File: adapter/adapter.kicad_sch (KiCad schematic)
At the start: 18 parts, among them J1 Conn_01x03_Female, J2 Conn_01x06_Female, SW1 RotaryEncoder_Switch

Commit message: routing, add R C
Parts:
- removed R2: R, Resistor_SMD:R_1206_3216Metric_Pad1.42x1.75mm_HandSolder, symbol Device:R
- C1: footprint Capacitor_SMD:C_1206_3216Metric_Pad1.42x1.75mm_HandSolder -> Capacitor_SMD:C_1206_3216Metric_Pad1.33x1.80mm_HandSolder
- R1: footprint Resistor_SMD:R_1206_3216Metric_Pad1.42x1.75mm_HandSolder -> Resistor_SMD:R_1206_3216Metric_Pad1.30x1.75mm_HandSolder
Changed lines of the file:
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@@
   (junction (at 118.11 102.87) (diameter 1.016) (color 0 0 0 0)
   )
-  (junction (at 73.914 95.25) (diameter 1.016) (color 0 0 0 0)
-  )
   (junction (at 30.226 34.29) (diameter 0) (color 0 0 0 0)
   )
@@
   )
   (junction (at 212.09 102.87) (diameter 0) (color 0 0 0 0)
-  )
-  (junction (at 81.534 95.25) (diameter 0) (color 0 0 0 0)
   )
   (junction (at 137.16 87.63) (diameter 0) (color 0 0 0 0)
@@
     (stroke (width 0) (type default) (color 0 0 0 0))
   )
-  (wire (pts (xy 81.534 97.79) (xy 81.534 95.25))
-    (stroke (width 0) (type solid) (color 0 0 0 0))
-  )
   (wire (pts (xy 88.9 87.63) (xy 97.79 87.63))
     (stroke (width 0) (type default) (color 0 0 0 0))
@@
   (wire (pts (xy 112.268 124.714) (xy 129.286 124.714))
     (stroke (width 0) (type default) (color 0 0 0 0))
-  )
-  (wire (pts (xy 73.914 95.25) (xy 73.914 97.79))
-    (stroke (width 0) (type solid) (color 0 0 0 0))
   )
   (wire (pts (xy 112.268 109.474) (xy 129.286 109.474))
@@
     (property "Reference" "R1" (id 0) (at 77.724 90.17 90))
     (property "Value" "R" (id 1) (at 77.724 92.71 90))
-    (property "Footprint" "Resistor_SMD:R_1206_3216Metric_Pad1.42x1.75mm_HandSolder" (id 2) (at 77.724 93.472 90)
+    (property "Footprint" "Resistor_SMD:R_1206_3216Metric_Pad1.30x1.75mm_HandSolder" (id 2) (at 77.724 93.472 90)
       (effects (font (size 1.27 1.27)) hide)
     )
@@
     (pin "1")
   )
-  (symbol (lib_id "Device:R") (at 77.724 97.79 270) (unit 1)
-    (in_bom yes) (on_board yes)
-    (property "Reference" "R2" (id 0) (at 77.724 92.71 90))
-    (property "Value" "R" (id 1) (at 77.724 95.25 90))
-    (property "Footprint" "Resistor_SMD:R_1206_3216Metric_Pad1.42x1.75mm_HandSolder" (id 2) (at 77.724 96.012 90)
-      (effects (font (size 1.27 1.27)) hide)
-    )
-    (property "Datasheet" "~" (id 3) (at 77.724 97.79 0)
-      (effects (font (size 1.27 1.27)) hide)
-    )
-    (pin "1")
-    (pin "2")
-  )
   (symbol (lib_id "power:+5V") (at 30.226 26.67 90) (unit 1)
     (in_bom yes) (on_board yes)
@@
       (effects (font (size 1.27 1.27)) (justify left))
     )
-    (property "Footprint" "Capacitor_SMD:C_1206_3216Metric_Pad1.42x1.75mm_HandSolder" (id 2) (at 37.5412 96.266 0)
+    (property "Footprint" "Capacitor_SMD:C_1206_3216Metric_Pad1.33x1.80mm_HandSolder" (id 2) (at 37.5412 96.266 0)
       (effects (font (size 1.27 1.27)) hide)
     )
@@
     )
     (path "/b720e53b-ae72-4295-b3ff-de5411507232"
-      (reference "C1") (unit 1) (value "1u") (footprint "Capacitor_SMD:C_1206_3216Metric_Pad1.42x1.75mm_HandSolder")
+      (reference "C1") (unit 1) (value "1u") (footprint "Capacitor_SMD:C_1206_3216Metric_Pad1.33x1.80mm_HandSolder")
     )
     (path "/223b04e8-40ea-4e7c-a2bb-67f20935b256"
@@
     )
     (path "/3145c452-dc50-487a-9802-6b13d8b48c50"
-      (reference "R1") (unit 1) (value "R") (footprint "Resistor_SMD:R_1206_3216Metric_Pad1.42x1.75mm_HandSolder")
-    )
-    (path "/890ed13f-42f7-4528-85cf-e8c0911e8d2e"
-      (reference "R2") (unit 1) (value "R") (footprint "Resistor_SMD:R_1206_3216Metric_Pad1.42x1.75mm_HandSolder")
+      (reference "R1") (unit 1) (value "R") (footprint "Resistor_SMD:R_1206_3216Metric_Pad1.30x1.75mm_HandSolder")
     )
     (path "/d31898a0-dde3-4548-9b2f-a263c96d031c"

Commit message: license
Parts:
- removed J1: Conn_01x03_Female, Connector_PinHeader_2.54mm:PinHeader_1x03_P2.54mm_Vertical, symbol Connector:Conn_01x03_Female
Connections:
- net GND: no longer C1.2, D1.2 (VSS), D10.2 (VSS), D11.2 (VSS), D12.2 (VSS), D2.2 (VSS), D3.2 (VSS), D4.2 (VSS), D5.2 (VSS), D6.2 (VSS), D7.2 (VSS), D8.2 (VSS), D9.2 (VSS)
- new net Gnd: C1.2, D1.2 (VSS), D10.2 (VSS), D11.2 (VSS), D12.2 (VSS), D2.2 (VSS), D3.2 (VSS), D4.2 (VSS), D5.2 (VSS), D6.2 (VSS), D7.2 (VSS), D8.2 (VSS), D9.2 (VSS)
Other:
- note added: "This work is licensed under a Creative Commons Attribution-NonCommercial-ShareAlike 4.0 International License."
- note removed: "RGB"
- company: BastardKB x KarlK90 -> BastardKB
- title: Charybdis Blackpill Holder -> Charybdis Rotary Encoder
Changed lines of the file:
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@@
   (paper "A4")
   (title_block
-    (title "Charybdis Blackpill Holder")
-    (date "2022-01-20")
-    (rev "1.2")
-    (company "BastardKB x KarlK90")
+    (title "Charybdis Rotary Encoder")
+    (date "2022-01-26")
+    (rev "1.0")
+    (company "BastardKB")
     (comment 1 "Licensed under CERN-OHL-W v2")
   )
@@
   )
   (junction (at 112.268 124.714) (diameter 0) (color 0 0 0 0)
-  )
-  (junction (at 26.162 73.66) (diameter 0) (color 0 0 0 0)
   )
   (junction (at 80.264 102.87) (diameter 0) (color 0 0 0 0)
@@
     (stroke (width 0) (type default) (color 0 0 0 0))
   )
-  (wire (pts (xy 26.162 73.66) (xy 34.29 73.66))
-    (stroke (width 0) (type default) (color 0 0 0 0))
-  )
-  (wire (pts (xy 26.162 73.66) (xy 26.162 75.184))
-    (stroke (width 0) (type default) (color 0 0 0 0))
-  )
   (wire (pts (xy 112.268 124.714) (xy 129.286 124.714))
     (stroke (width 0) (type default) (color 0 0 0 0))
@@
     (stroke (width 0) (type default) (color 0 0 0 0))
   )
-  (wire (pts (xy 24.13 73.66) (xy 26.162 73.66))
-    (stroke (width 0) (type default) (color 0 0 0 0))
-  )
   (wire (pts (xy 137.16 102.87) (xy 154.94 102.87))
     (stroke (width 0) (type default) (color 0 0 0 0))
@@
     (effects (font (size 1.27 1.27)) (justify left bottom))
   )
-  (text "RGB" (at 21.59 67.31 0)
-    (effects (font (size 1.27 1.27)) (justify left bottom))
+  (text "This work is licensed under a Creative Commons Attribution-NonCommercial-ShareAlike 4.0 International License."
+    (at 279.4 163.83 0)
+    (effects (font (size 1.27 1.27)) (justify right bottom))
   )
   (global_label "Vcc" (shape input) (at 26.924 34.29 180)
@@
     )
   )
-  (global_label "Din" (shape input) (at 34.29 76.2 180)
-    (effects (font (size 1.27 1.27)) (justify right))
-    (property "Intersheet References" "${INTERSHEET_REFS}" (id 0) (at -2.54 2.54 0)
-      (effects (font (size 1.27 1.27)) hide)
-    )
-  )
   (global_label "r1" (shape input) (at 92.71 35.56 0) (fields_autoplaced)
     (effects (font (size 1.1938 1.1938)) (justify left))
@@
     )
   )
-  (global_label "Vcc" (shape input) (at 34.29 71.12 180)
-    (effects (font (size 1.27 1.27)) (justify right))
-    (property "Intersheet References" "${INTERSHEET_REFS}" (id 0) (at -2.54 2.54 0)
-      (effects (font (size 1.27 1.27)) hide)
-    )
-  )
   (global_label "Vcc" (shape input) (at 30.734 87.884 180)
     (effects (font (size 1.27 1.27)) (justify right))
     (property "Intersheet References" "${INTERSHEET_REFS}" (id 0) (at -6.096 19.304 0)
-      (effects (font (size 1.27 1.27)) hide)
-    )
-  )
-  (global_label "Gnd" (shape input) (at 24.13 73.66 180)
-    (effects (font (size 1.27 1.27)) (justify right))
-    (property "Intersheet References" "${INTERSHEET_REFS}" (id 0) (at -12.7 2.54 0)
       (effects (font (size 1.27 1.27)) hide)
     )
@@
     (pin "1")
   )
-  (symbol (lib_id "power:GND") (at 26.162 75.184 0) (unit 1)
-    (in_bom yes) (on_board yes)
-    (property "Reference" "#PWR0104" (id 0) (at 26.162 81.534 0)
-      (effects (font (size 1.27 1.27)) hide)
-    )
-    (property "Value" "GND" (id 1) (at 26.162 78.994 0))
-    (property "Footprint" "" (id 2) (at 26.162 75.184 0)
-      (effects (font (size 1.27 1.27)) hide)
-    )
-    (property "Datasheet" "" (id 3) (at 26.162 75.184 0)
-      (effects (font (size 1.27 1.27)) hide)
-    )
-    (pin "1")
-  )
   (symbol (lib_id "Device:C") (at 36.576 92.456 0) (unit 1)
     (in_bom yes) (on_board yes)
@@
     (pin "S2")
   )
-  (symbol (lib_id "Connector:Conn_01x03_Female") (at 39.37 73.66 0) (unit 1)
-    (in_bom yes) (on_board yes)
-    (property "Reference" "J1" (id 0) (at 40.0813 72.9678 0)
-      (effects (font (size 1.27 1.27)) (justify left))
-    )
-    (property "Value" "Conn_01x03_Female" (id 1) (at 40.0813 75.2665 0)
-      (effects (font (size 1.27 1.27)) (justify left))
-    )
-    (property "Footprint" "Connector_PinHeader_2.54mm:PinHeader_1x03_P2.54mm_Vertical" (id 2) (at 39.37 73.66 0)
-      (effects (font (size 1.27 1.27)) hide)
-    )
-    (property "Datasheet" "~" (id 3) (at 39.37 73.66 0)
-      (effects (font (size 1.27 1.27)) hide)
-    )
-    (pin "1")
-    (pin "2")
-    (pin "3")
-  )
   (symbol (lib_id "power:GND") (at 75.946 41.402 0) (unit 1)
     (in_bom yes) (on_board yes)
@@
       (reference "#PWR0103") (unit 1) (value "GND") (footprint "")
     )
-    (path "/9fc3e7de-917d-471e-9baf-20e418f20549"
-      (reference "#PWR0104") (unit 1) (value "GND") (footprint "")
-    )
     (path "/f298f139-b4e7-4161-948f-e52265423988"
       (reference "#PWR0105") (unit 1) (value "GND") (footprint "")
@@
       (reference "D12") (unit 1) (value "SK6812MINI") (footprint "Library:YS-SK6812MINI-E")
     )
-    (path "/eb54f150-1815-419c-99e6-8c3c5774df70"
-      (reference "J1") (unit 1) (value "Conn_01x03_Female") (footprint "Connector_PinHeader_2.54mm:PinHeader_1x03_P2.54mm_Vertical")
-    )
     (path "/26af3975-a636-45c1-8b88-2ae79f76cdc4"

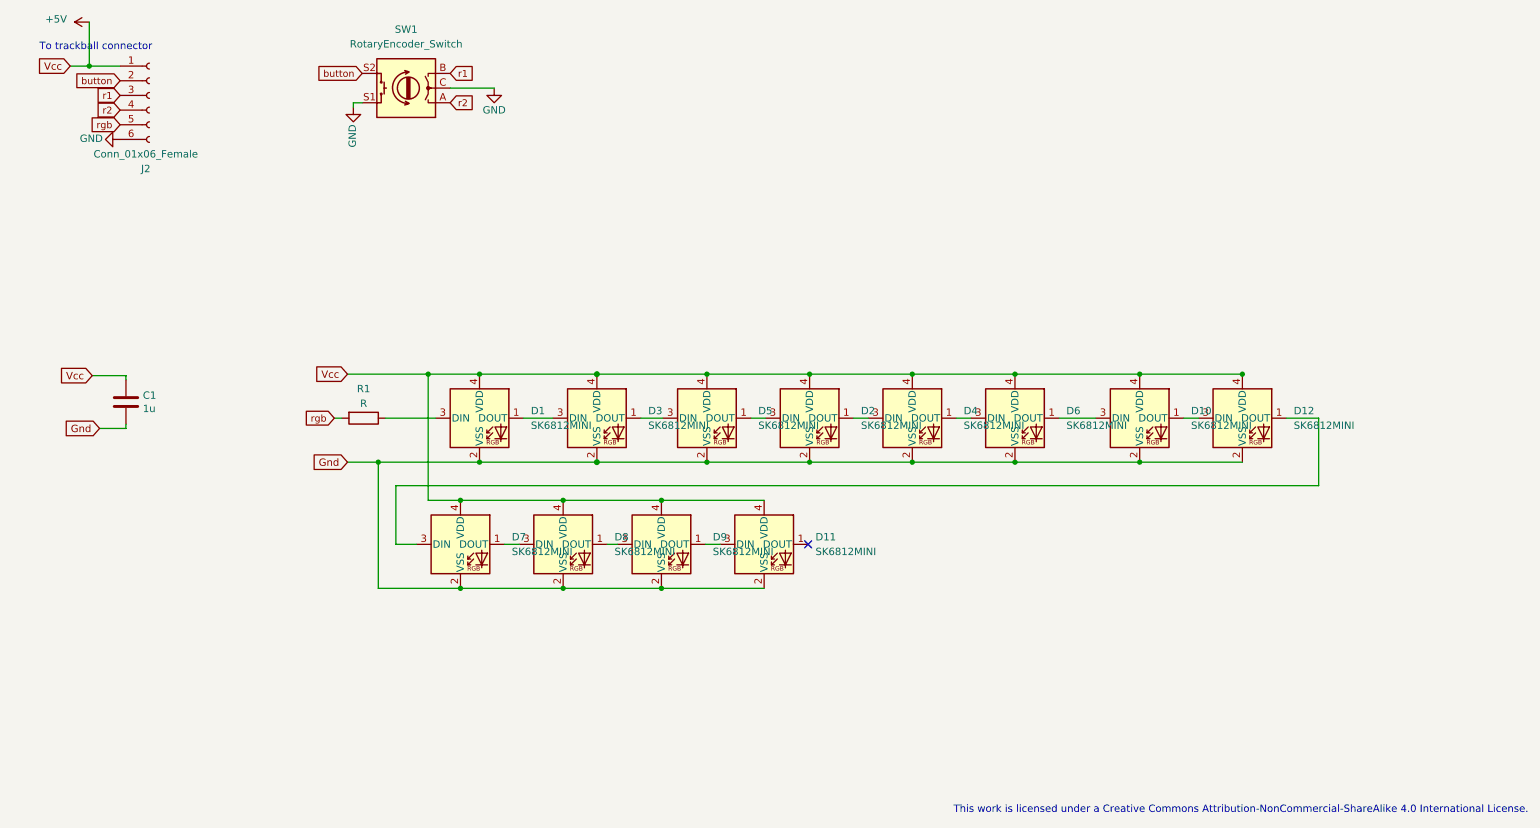
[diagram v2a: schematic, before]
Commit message: complete reroute
- routing changed to fix din/dout paths
- added dout header
- renamed rgb header to din
- moved SMT components to bottom side
- changed silkscreen to rev 1.1
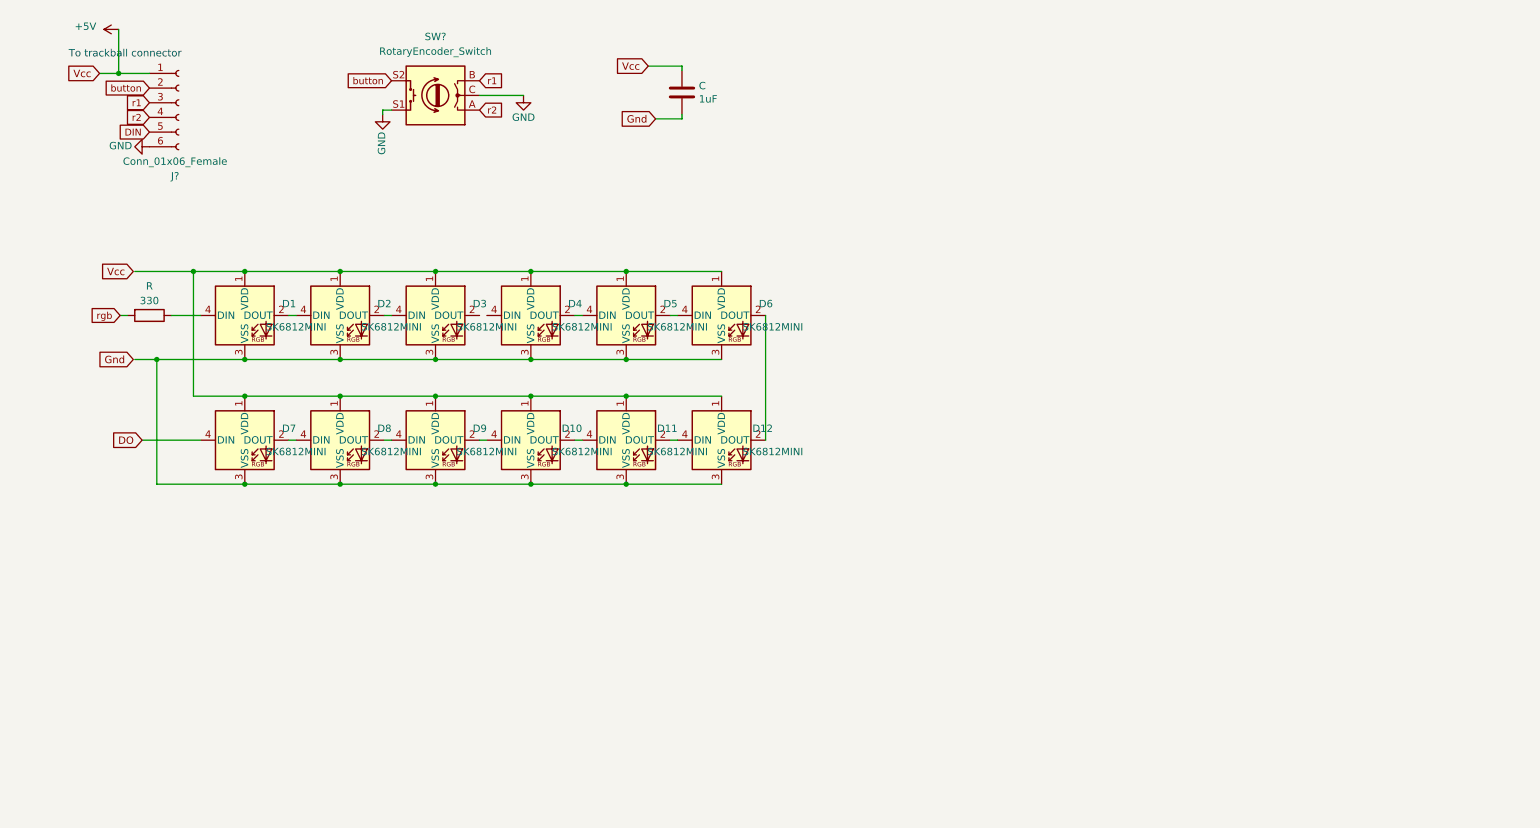
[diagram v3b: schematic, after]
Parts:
- removed C1: 1u, Capacitor_SMD:C_1206_3216Metric_Pad1.33x1.80mm_HandSolder, symbol Device:C
- removed J2: Conn_01x06_Female, Library:6_PinHeader, symbol Connector:Conn_01x06_Female
- removed R1: R, Resistor_SMD:R_1206_3216Metric_Pad1.30x1.75mm_HandSolder, symbol Device:R
- removed SW1: RotaryEncoder_Switch, Library:RotaryEncoder_Alps_EC11E-Switch_Vertical_H20mm, symbol Device:RotaryEncoder_Switch
- added C: 1uF, Capacitor_SMD:C_1206_3216Metric_Pad1.33x1.80mm_HandSolder, symbol Device:C
- added J?: Conn_01x06_Female, Library:6_PinHeader, symbol Connector:Conn_01x06_Female
- added R: 330, Resistor_SMD:R_1206_3216Metric_Pad1.30x1.75mm_HandSolder, symbol Device:R
- added SW?: RotaryEncoder_Switch, Library:RotaryEncoder_Alps_EC11E-Switch_Vertical_H20mm, symbol Device:RotaryEncoder_Switch
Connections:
- net +5V: now also C.1, J?.1 (Pin_1); no longer D1.4 (VDD), D10.4 (VDD), D11.4 (VDD), D12.4 (VDD), D2.4 (VDD), D3.4 (VDD), D4.4 (VDD), D5.4 (VDD), D6.4 (VDD), D7.4 (VDD), D8.4 (VDD), D9.4 (VDD)
- net GND: now also J?.6 (Pin_6), SW?.C, SW?.S1
- net Gnd: now also C.2; no longer D1.2 (VSS), D10.2 (VSS), D11.2 (VSS), D12.2 (VSS), D2.2 (VSS), D3.2 (VSS), D4.2 (VSS), D5.2 (VSS), D6.2 (VSS), D7.2 (VSS), D8.2 (VSS), D9.2 (VSS)
- net button: now also J?.2 (Pin_2), SW?.S2
- net r1: now also J?.3 (Pin_3), SW?.B
- net r2: now also J?.4 (Pin_4), SW?.A
- net rgb: now also R.2
- net at D12.1 (VDD): now also D1.1 (VDD), D10.1 (VDD), D11.1 (VDD), D2.1 (VDD), D3.1 (VDD), D4.1 (VDD), D5.1 (VDD), D6.1 (VDD), D7.1 (VDD), D8.1 (VDD), D9.1 (VDD); no longer D7.3 (DIN)
- net at D12.3 (VSS): now also D1.3 (VSS), D10.3 (VSS), D11.3 (VSS), D2.3 (VSS), D3.3 (VSS), D4.3 (VSS), D5.3 (VSS), D6.3 (VSS), D7.3 (VSS), D8.3 (VSS), D9.3 (VSS); no longer D10.1 (DOUT)
- new net: D10.2 (DOUT), D11.4 (DIN)
- new net: D10.4 (DIN), D9.2 (DOUT)
- new net: D1.4 (DIN), R.1
- new net: D8.2 (DOUT), D9.4 (DIN)
- new net: D7.2 (DOUT), D8.4 (DIN)
- new net: D11.2 (DOUT), D12.4 (DIN)
- new net: D5.2 (DOUT), D6.4 (DIN)
- new net: D4.2 (DOUT), D5.4 (DIN)
- new net: D12.2 (DOUT), D6.2 (DOUT)
- new net: D2.2 (DOUT), D3.4 (DIN)
- new net: D1.2 (DOUT), D2.4 (DIN)
- new net DIN: J?.5 (Pin_5)
- new net DO: D7.4 (DIN)
- no-connect marks 1 -> 0
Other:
- note removed: "This work is licensed under a Creative Commons Attribution-NonCommercial-ShareAlike 4.0 International License."
- company: BastardKB -> (none)
- title: Charybdis Rotary Encoder -> (none)
